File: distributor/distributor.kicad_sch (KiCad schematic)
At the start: 34 parts, among them J1 Cerebellum, J10 CAN FD, J11 CAN FD, J12 CAN FD, J13 CAN FD, J14 ArmR, J15 CAN FD, J16 ArmL, J2 Cerebrum, J3 PowerBack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

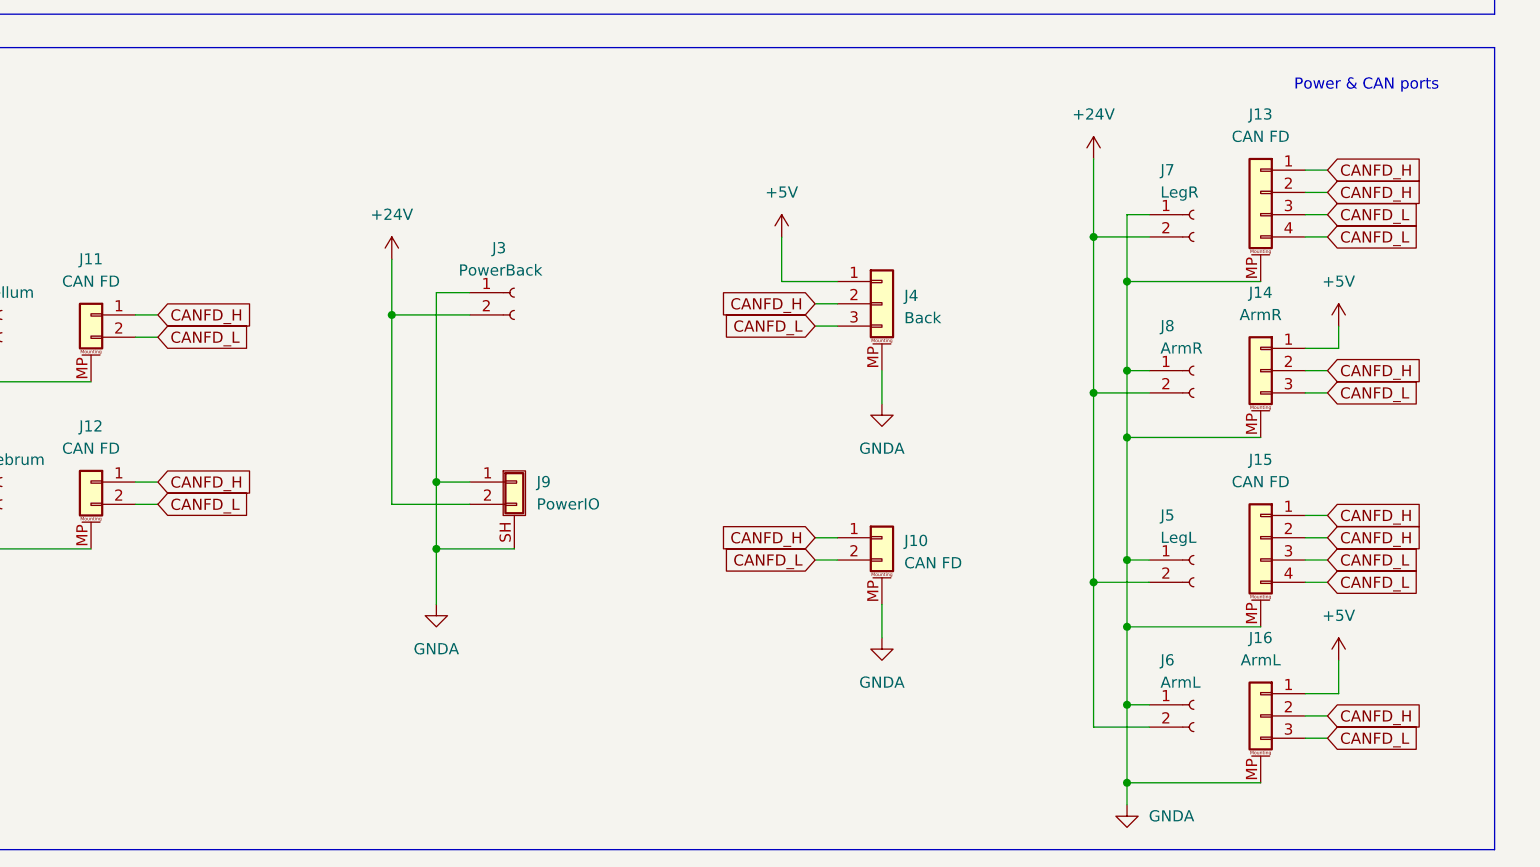
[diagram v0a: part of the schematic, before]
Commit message: [Modify] Change CAN ports sequence
2pin: 1-CAN_L, 2-CAN_H
3pin: 1-5V, 2-CAN_L, 3-CAN_H
4pin: 1,2-CAN_L, 3,4-CAN_H

Signed-off-by: Homalozoa <nx.tardis@gmail.com>
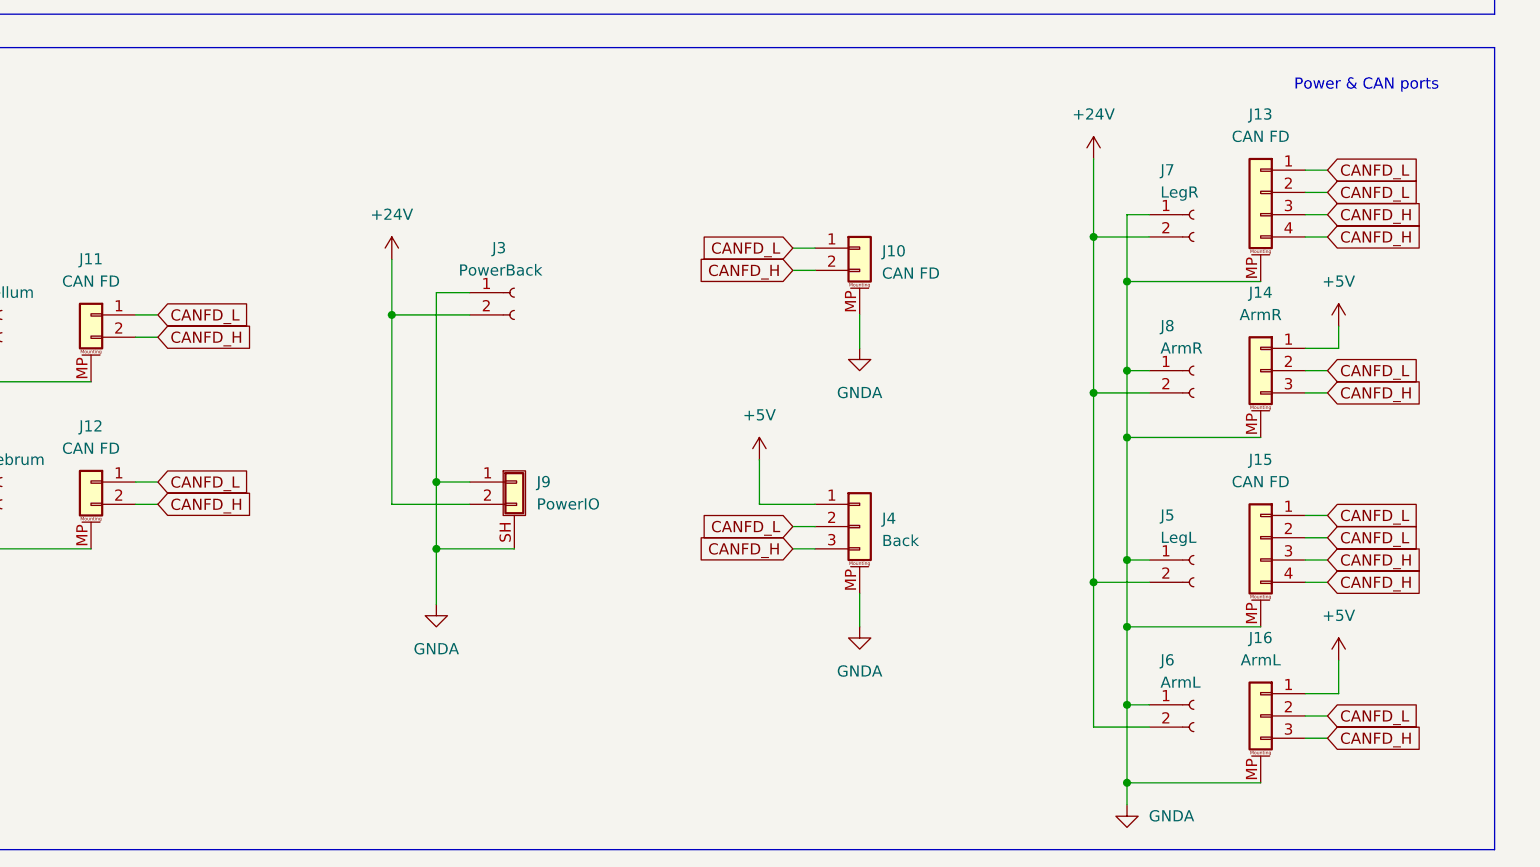
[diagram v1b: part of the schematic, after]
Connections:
- net CANFD_H: now also J10.2 (Pin_2), J11.2 (Pin_2), J12.2 (Pin_2), J13.3 (Pin_3), J13.4 (Pin_4), J14.3 (Pin_3), J15.3 (Pin_3), J15.4 (Pin_4), J16.3 (Pin_3), J4.3 (Pin_3); no longer J10.1 (Pin_1), J11.1 (Pin_1), J12.1 (Pin_1), J13.1 (Pin_1), J13.2 (Pin_2), J14.2 (Pin_2), J15.1 (Pin_1), J15.2 (Pin_2), J16.2 (Pin_2), J4.2 (Pin_2)
- net CANFD_L: now also J10.1 (Pin_1), J11.1 (Pin_1), J12.1 (Pin_1), J13.1 (Pin_1), J13.2 (Pin_2), J14.2 (Pin_2), J15.1 (Pin_1), J15.2 (Pin_2), J16.2 (Pin_2), J4.2 (Pin_2); no longer J10.2 (Pin_2), J11.2 (Pin_2), J12.2 (Pin_2), J13.3 (Pin_3), J13.4 (Pin_4), J14.3 (Pin_3), J15.3 (Pin_3), J15.4 (Pin_4), J16.3 (Pin_3), J4.3 (Pin_3)
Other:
- moved on the sheet: J10, J4
